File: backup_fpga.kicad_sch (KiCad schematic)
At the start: 1 part, among them U7 LFE5U-12F-7BG381x

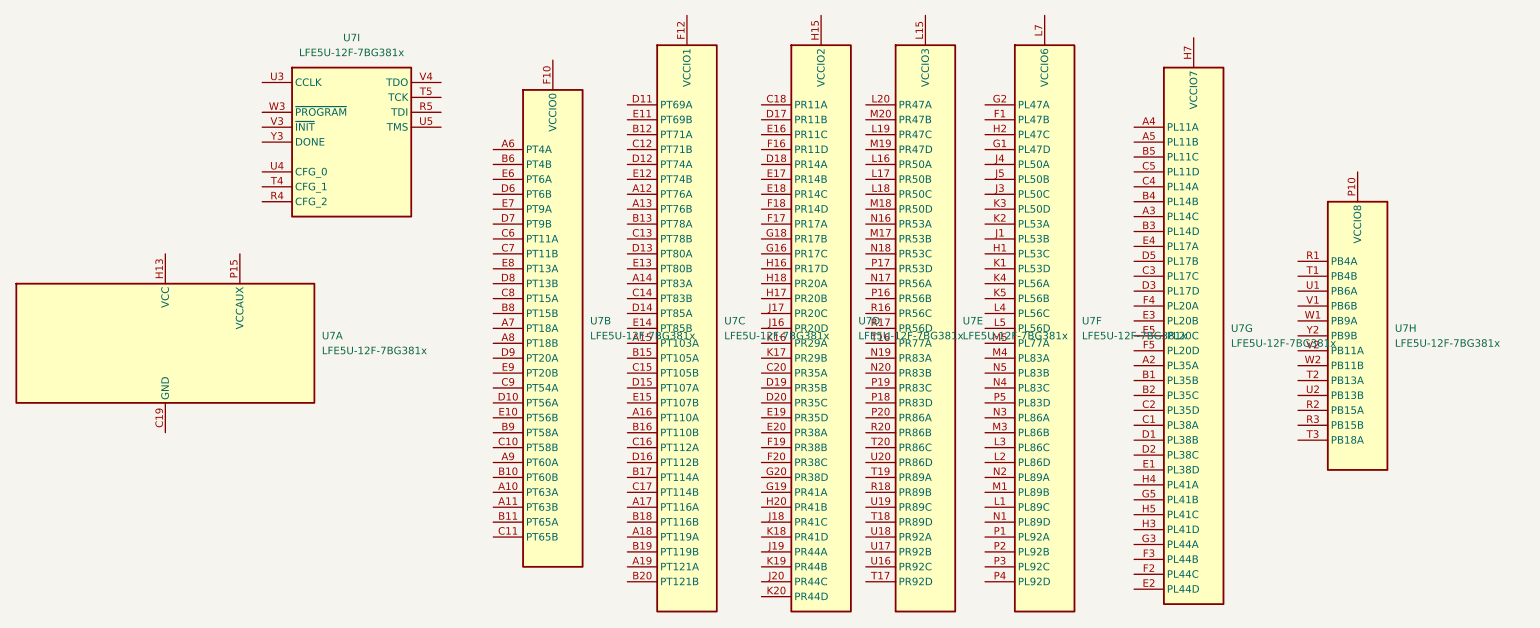
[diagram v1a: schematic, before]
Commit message: mark all extra pins as no-connect. erc fixed.
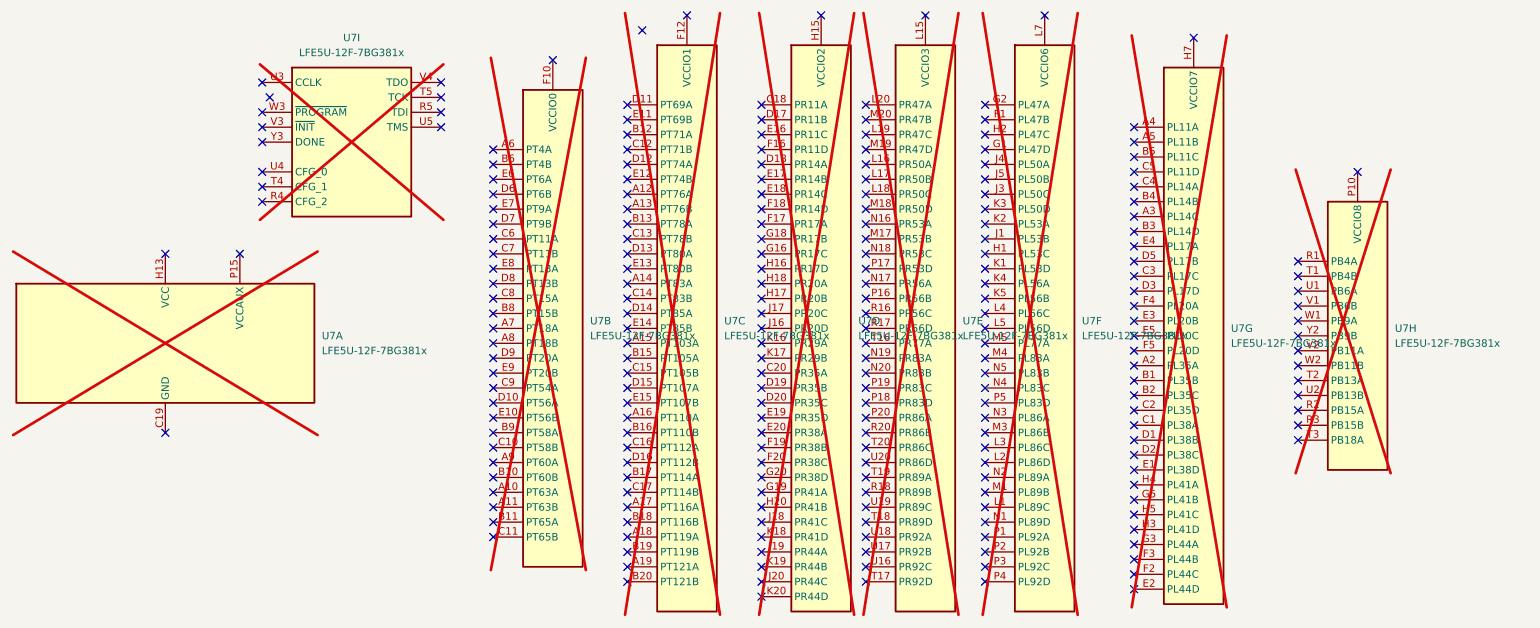
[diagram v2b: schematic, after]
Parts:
- U7: now not fitted
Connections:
- no-connect marks 0 -> 228

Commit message: interim esp32 change
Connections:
- no-connect marks 228 -> 226
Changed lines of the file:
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@@
-	)
-	(no_connect
-		(at 132.08 36.83)
 	)
 	(no_connect
@@
 	)
 	(no_connect
-		(at 68.58 48.26)
-	)
-	(no_connect
